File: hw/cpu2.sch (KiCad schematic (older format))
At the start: 0 parts

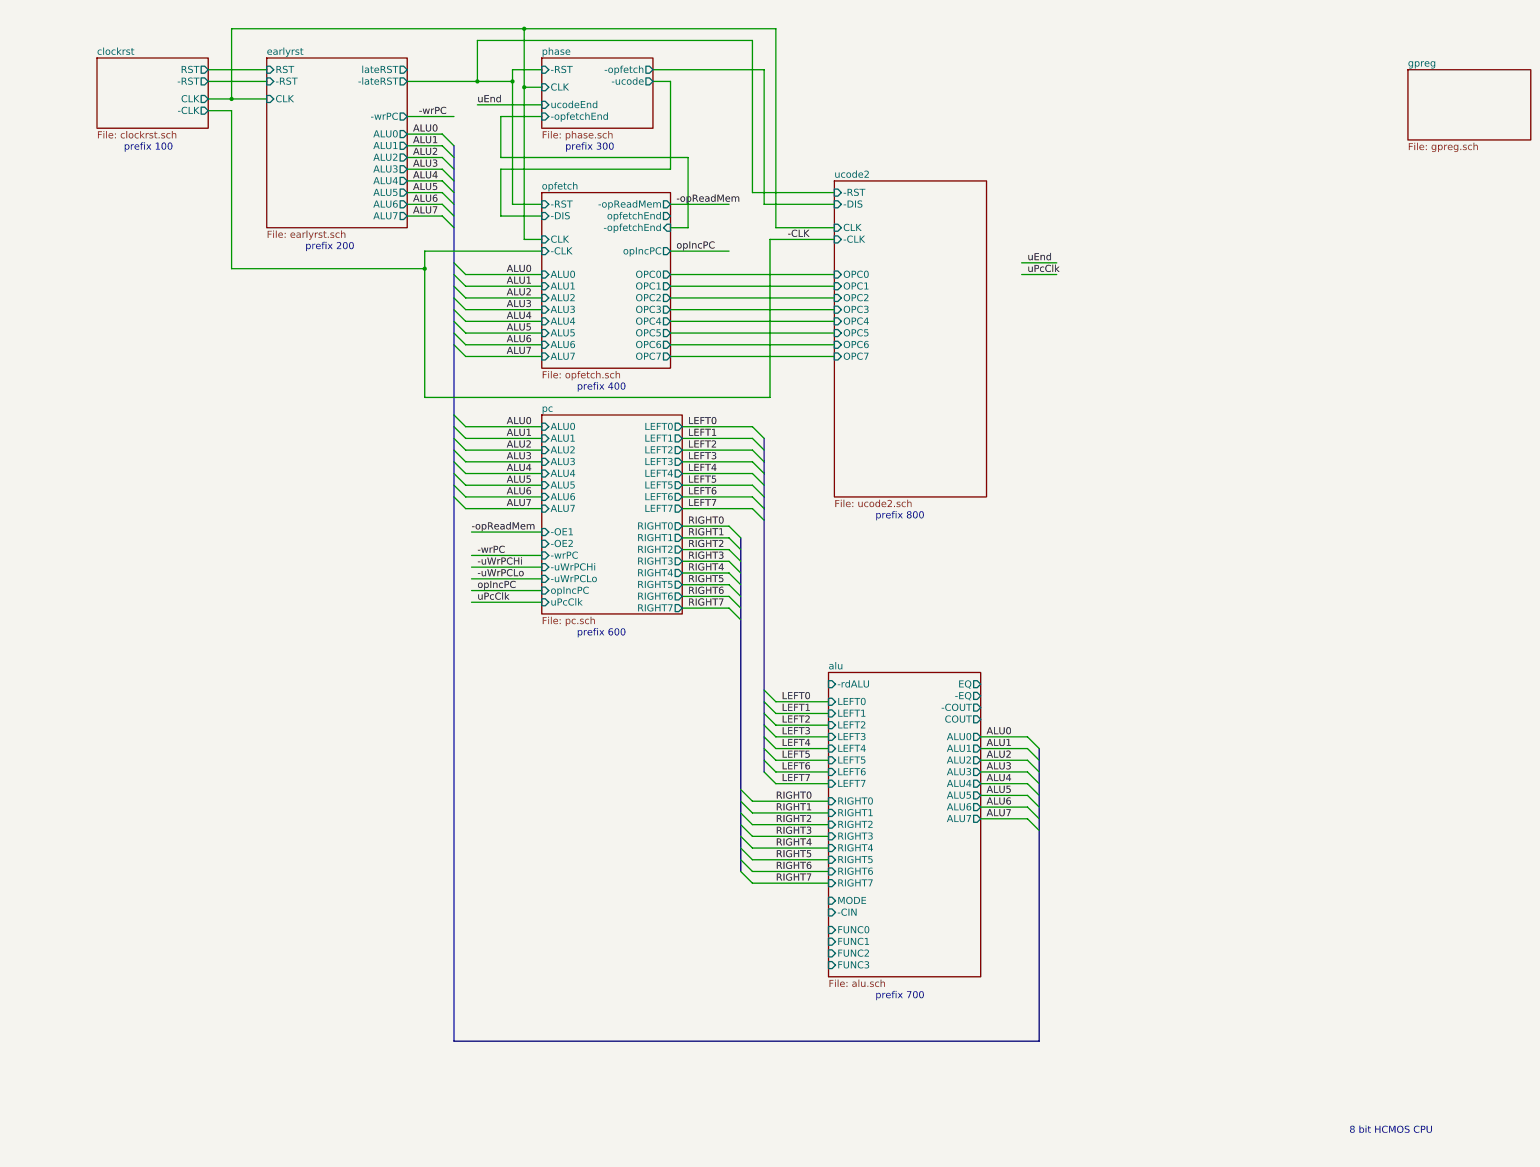
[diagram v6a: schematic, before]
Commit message: clean up top-level schematic
Just label inputs and outputs to each module.
Running wires everywhere is just confusing.
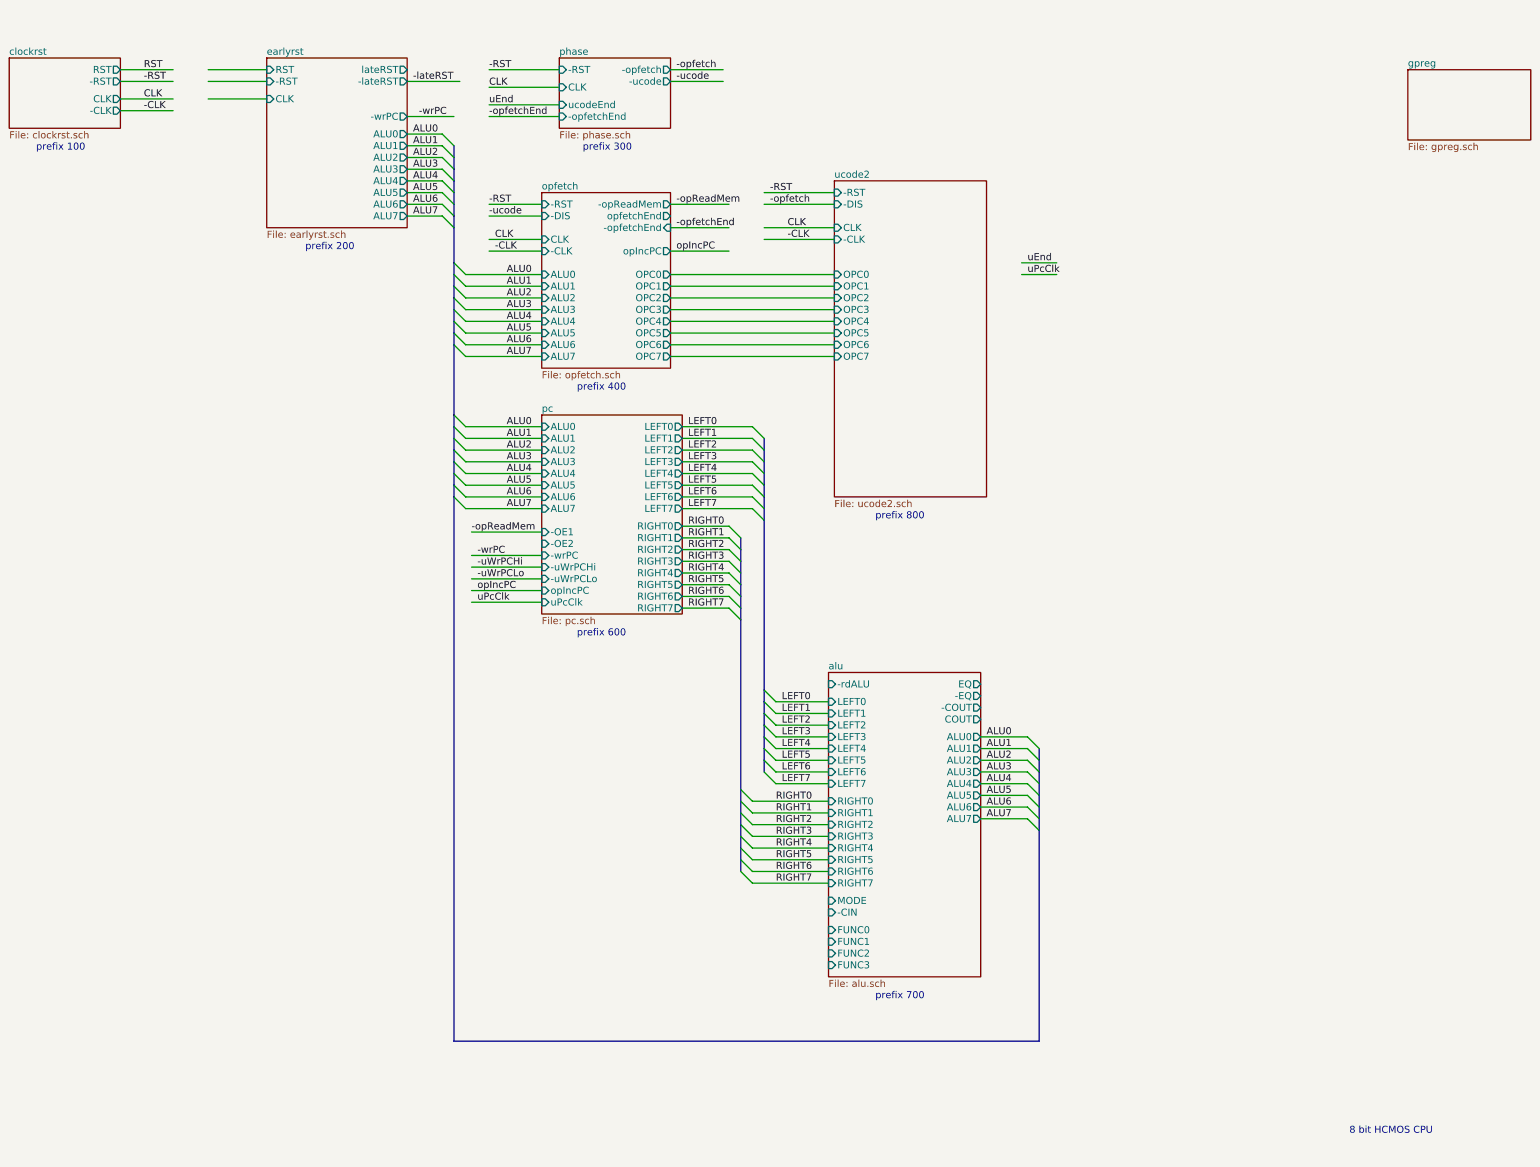
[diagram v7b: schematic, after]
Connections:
- net labels added: -RST, -lateRST, -opfetch, -opfetchEnd, -ucode, CLK, RST
- wire segments 123 -> 106

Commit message: implement GP registers
Also, add ucode signals to main sheet, and do
some cleanup on main sheet.
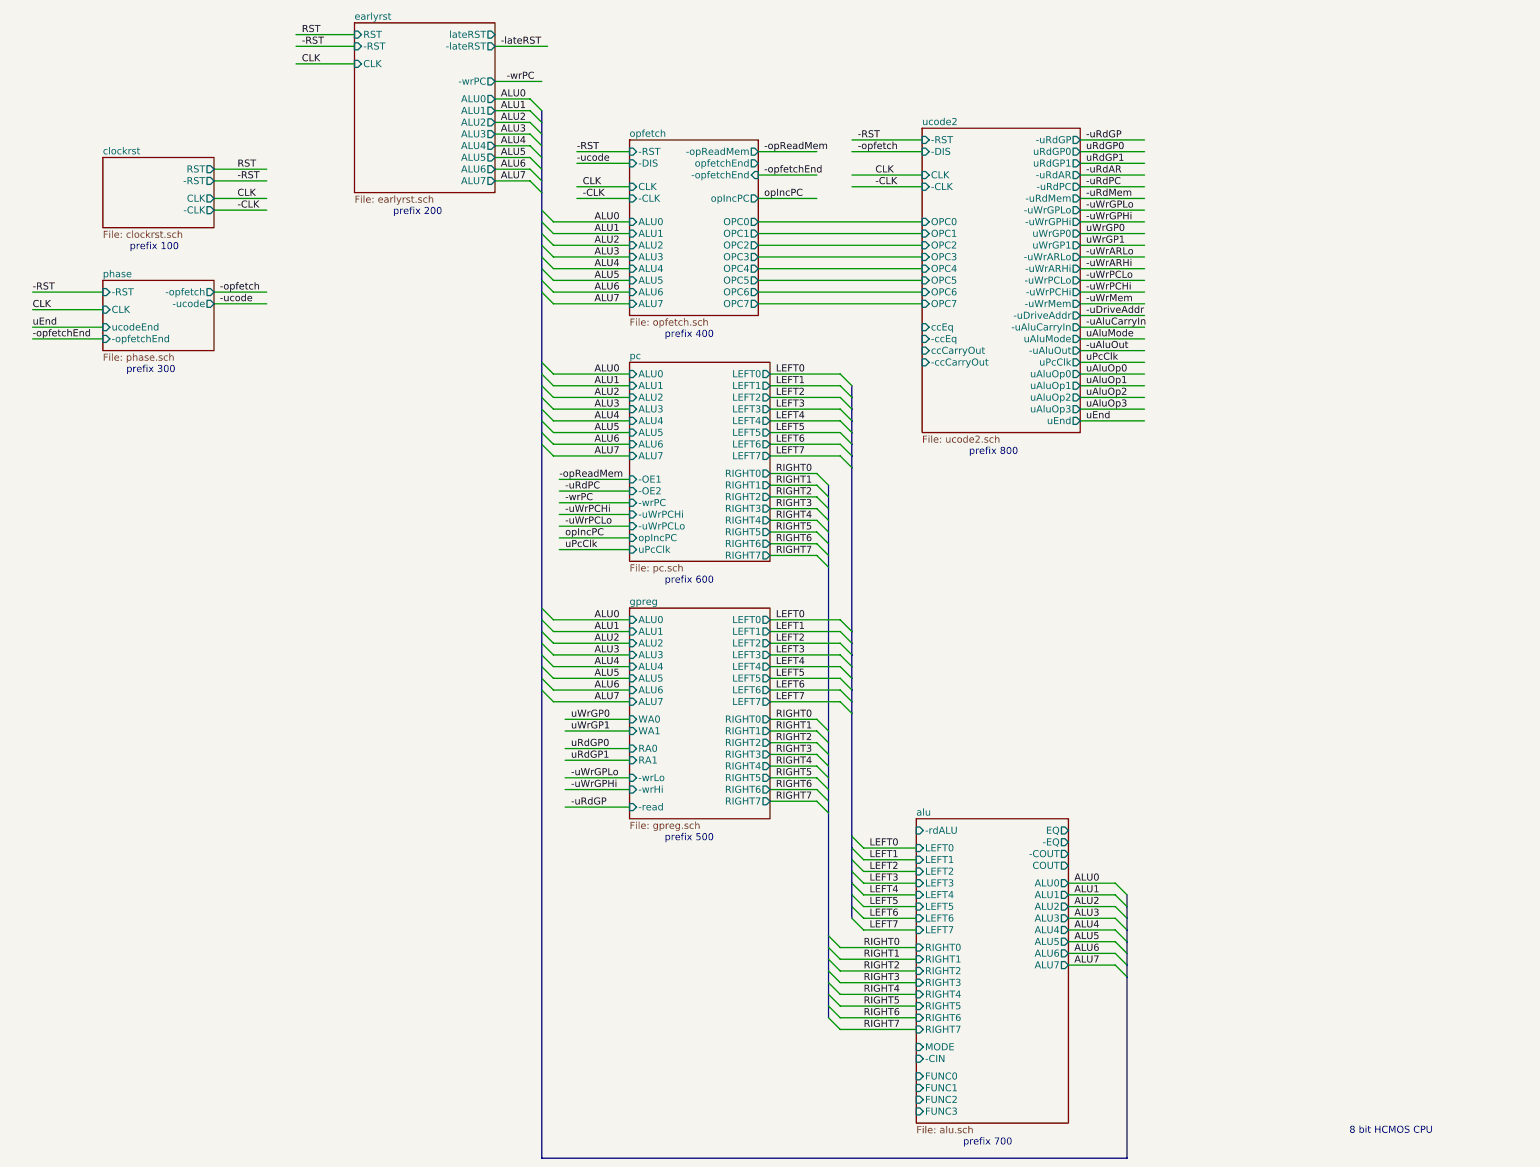
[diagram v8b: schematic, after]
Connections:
- net labels added: -uAluCarryIn, -uAluOut, -uDriveAddr, -uRdAR, -uRdGP, -uRdMem, -uRdPC, -uWrARHi, -uWrARLo, -uWrGPHi, -uWrGPLo, -uWrMem, uAluMode, uAluOp0, uAluOp1, uAluOp2, uAluOp3, uRdGP0, uRdGP1, uWrGP0, uWrGP1
- wire segments 106 -> 161
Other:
- note added: "prefix 500"
